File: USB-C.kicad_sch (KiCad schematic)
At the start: 11 parts, among them J1 USB_C_Receptacle_USB2.0_16P, U6 TPD2E001DRYR, U9 TPS25200DRVR

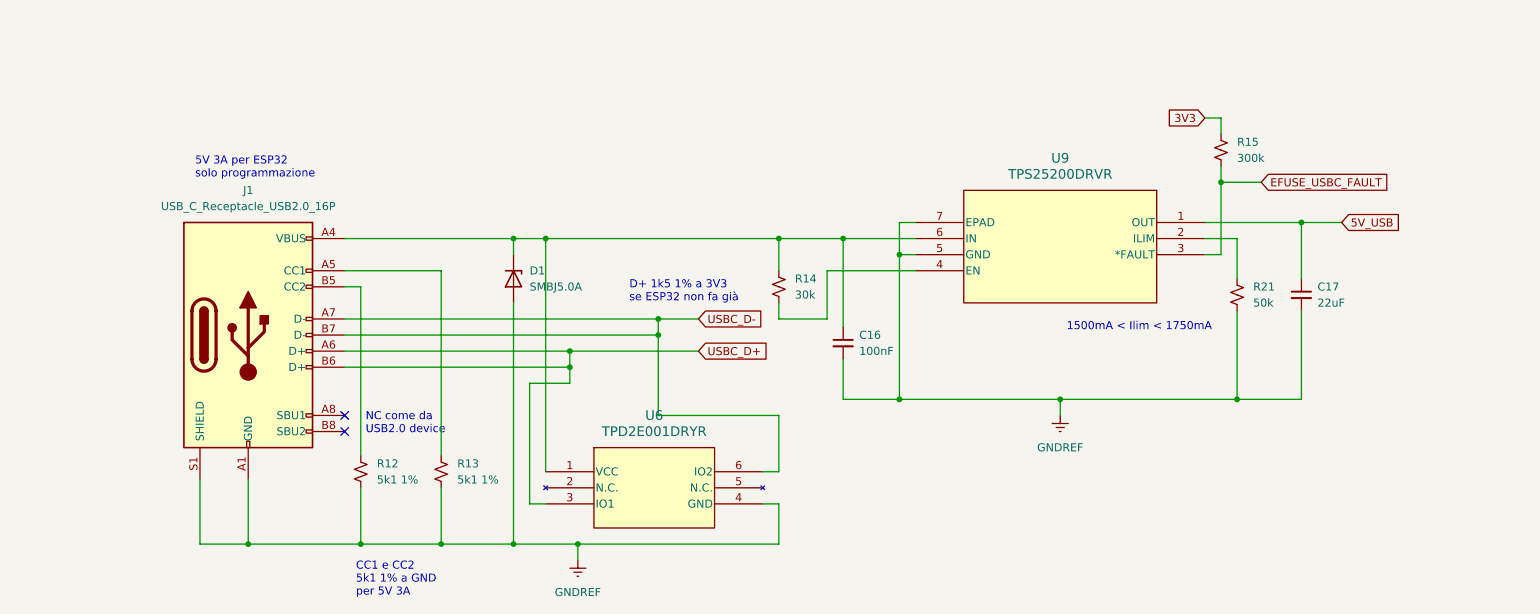
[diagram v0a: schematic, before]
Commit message: updated components and nets
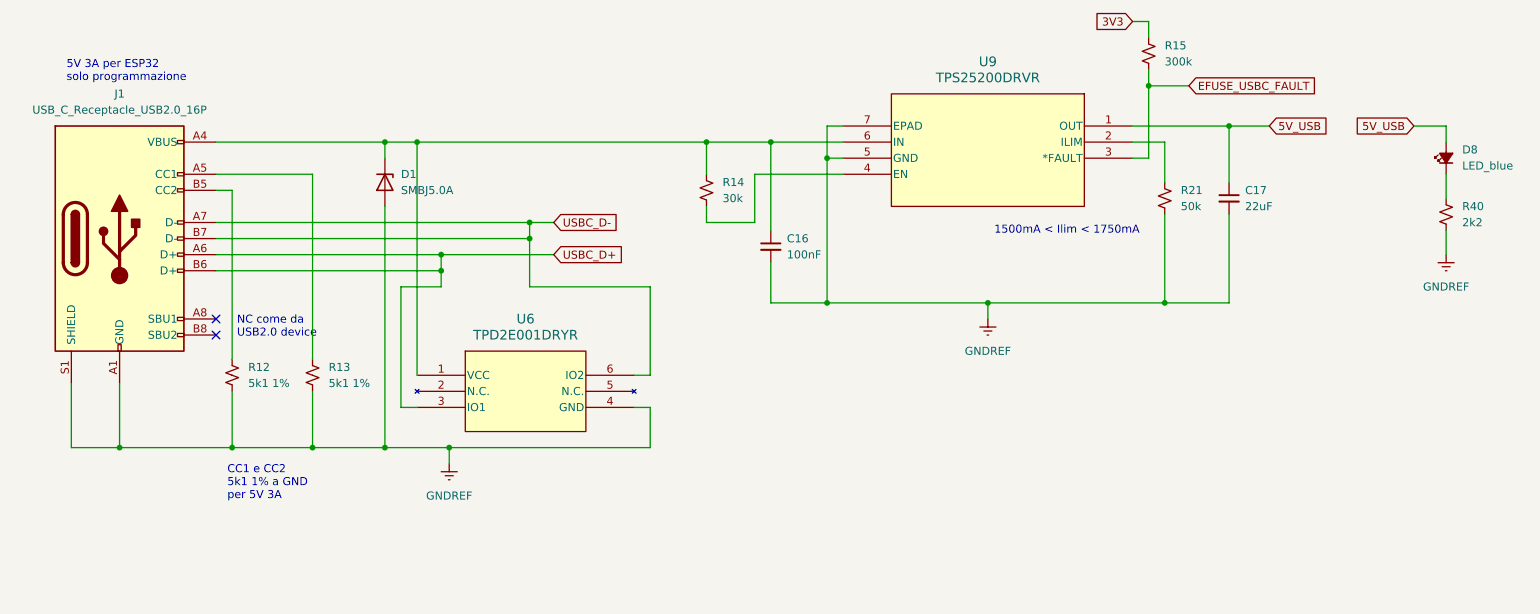
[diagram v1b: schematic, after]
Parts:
- added D8: LED_blue, symbol Device:LED_Small_Filled
- added R40: 2k2, symbol Device:R_Small_US
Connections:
- net 5V_USB: now also D8.2 (A)
- net GNDREF: now also R40.2
- new net: D8.1 (K), R40.1
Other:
- note removed: "D+ 1k5 1% a 3V3 se ESP32 non fa già"
- moved on the sheet: C16, C17, D1, J1, R12, R13, R14, R15, R21, U6, U9
